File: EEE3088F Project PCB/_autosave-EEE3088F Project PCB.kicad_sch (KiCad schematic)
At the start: 80 parts, among them J1 JST PH 2.00mm connector, Q1 NPN, SW1 SS-12D10L3, U1 DRV8833PWR, U10 LM7805L-TF3-T, U11 TC4056A., U2 DRV8833PWPR, U3 INA219AxD, U4 CH224K, U6 MIC5504-1.2YM5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

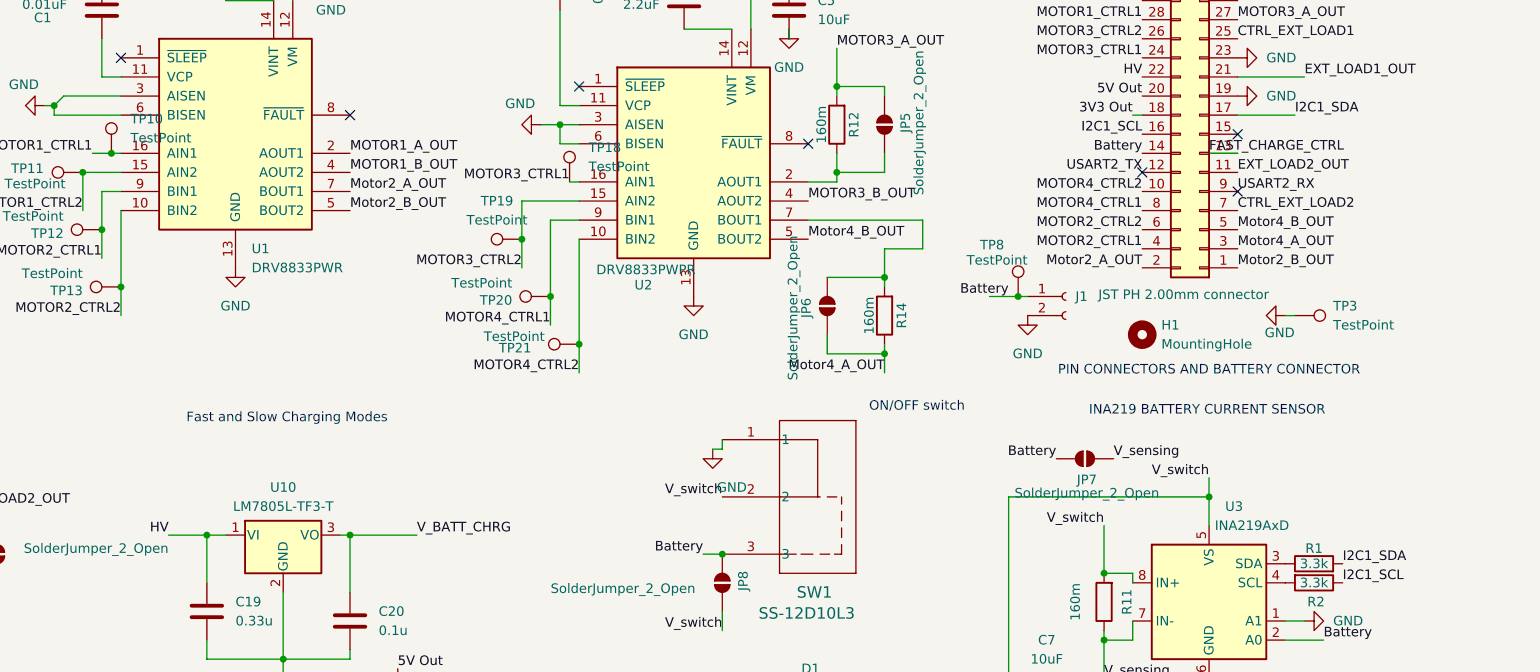
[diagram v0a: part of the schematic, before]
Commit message: completed the first iteration where all routing is completed
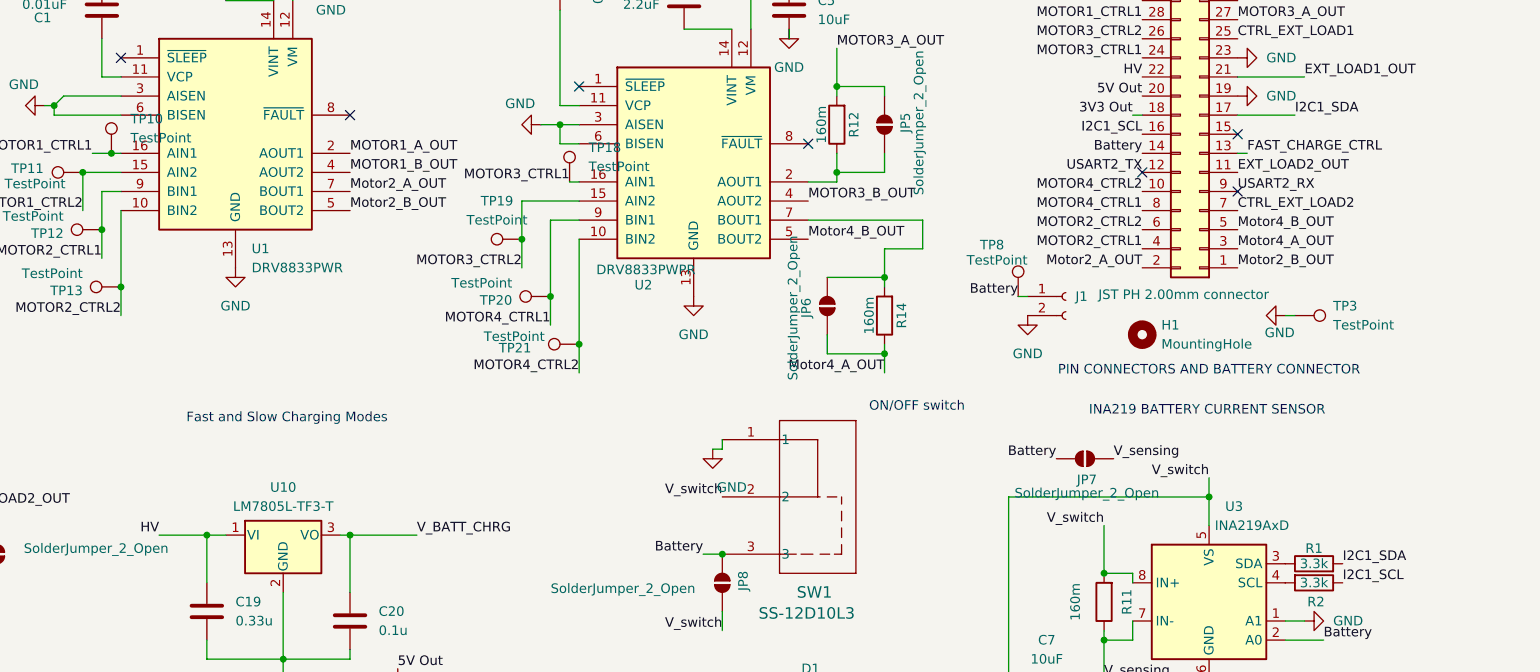
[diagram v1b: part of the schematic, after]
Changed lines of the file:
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@@
 	)
 	(junction
-		(at 232.41 67.31)
-		(diameter 0)
-		(color 0 0 0 0)
-	)
-	(junction
 		(at 86.36 128.27)
 		(diameter 0)
@@
 	(wire
 		(pts
-			(xy 228.6 67.31) (xy 232.41 67.31)
-		)
-		(stroke
-			(width 0)
-			(type default)
-		)
-	)
-	(wire
-		(pts
 			(xy 271.78 139.7) (xy 269.24 139.7)
 		)
@@
 	(wire
 		(pts
-			(xy 119.38 99.06) (xy 124.46 99.06)
+			(xy 118.11 99.06) (xy 124.46 99.06)
 		)
 		(stroke
@@
 	(wire
 		(pts
-			(xy 261.62 48.26) (xy 257.81 48.26)
+			(xy 261.62 48.26) (xy 262.89 48.26)
 		)
 		(stroke
@@
 	)
 	(label "HV"
-		(at 119.38 99.06 180)
+		(at 118.11 99.06 180)
 		(effects
 			(font
@@
 	)
 	(label "Battery"
-		(at 231.14 67.31 180)
+		(at 232.41 67.31 180)
 		(effects
 			(font
@@
 	)
 	(label "FAST_CHARGE_CTRL"
-		(at 257.81 48.26 0)
+		(at 262.89 48.26 0)
 		(effects
 			(font
@@
 		(polyline
 			(pts
-				(xy 93.98 12.7) (xy 93.98 78.74) (xy 222.25 78.74) (xy 222.25 12.7)
+				(xy 222.25 12.7) (xy 222.25 78.74) (xy 284.48 78.74) (xy 284.48 12.7)
 			)
 			(stroke
@@
 		(polyline
 			(pts
-				(xy 12.7 78.74) (xy 11.43 153.67) (xy 106.68 152.7175) (xy 106.68 78.4225)
+				(xy 167.64 78.74) (xy 167.64 114.3) (xy 228.6 114.3) (xy 228.6 78.74)
 			)
 			(stroke
@@
 		(polyline
 			(pts
-				(xy 167.64 78.74) (xy 167.64 114.3) (xy 228.6 114.3) (xy 228.6 78.74)
+				(xy 12.7 78.74) (xy 11.43 153.67) (xy 106.68 152.7175) (xy 106.68 78.4225)
 			)
 			(stroke
@@
 		(polyline
 			(pts
-				(xy 222.25 12.7) (xy 222.25 78.74) (xy 284.48 78.74) (xy 284.48 12.7)
+				(xy 93.98 12.7) (xy 93.98 78.74) (xy 222.25 78.74) (xy 222.25 12.7)
 			)
 			(stroke
